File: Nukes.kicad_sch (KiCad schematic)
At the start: 25 parts, among them J12 Conn_01x05_Male, J6 Screw_Terminal_01x08, Q3 NCV8415STT1G, Q4 NCV8415STT1G, Q5 NCV8415STT1G, Q6 NCV8415STT1G, U4 LTV-247, U5 PCA9534RGVR, U6 PCA9685BS

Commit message: v2 time
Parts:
- C17: renamed from C7; footprint Capacitor_SMD:C_0603_1608Metric -> Capacitor_SMD:C_0402_1005Metric
- C18: renamed from C8; footprint Capacitor_SMD:C_0603_1608Metric -> Capacitor_SMD:C_0402_1005Metric
- C19: renamed from C9; footprint Capacitor_SMD:C_0603_1608Metric -> Capacitor_SMD:C_0402_1005Metric
- C20: renamed from C10; footprint Capacitor_SMD:C_0603_1608Metric -> Capacitor_SMD:C_0402_1005Metric
- D10: renamed from D8; footprint Diode_SMD:D_SOD-128 -> Package_TO_SOT_SMD:TO-277B
- D7: renamed from D16; footprint Diode_SMD:D_SOD-128 -> Package_TO_SOT_SMD:TO-277B
- D8: renamed from D10; footprint Diode_SMD:D_SOD-128 -> Package_TO_SOT_SMD:TO-277B
- D9: renamed from D15; footprint Diode_SMD:D_SOD-128 -> Package_TO_SOT_SMD:TO-277B
- renumbered J12 to J7, Q6 to Q2, Q4 to Q3, Q5 to Q4, Q3 to Q5, R34 to R17, R26 to R18, R36 to R19, R29 to R20, R33 to R21, R25 to R22, R27 to R23, R35 to R24, U4 to U3, U5 to U4, U6 to U5

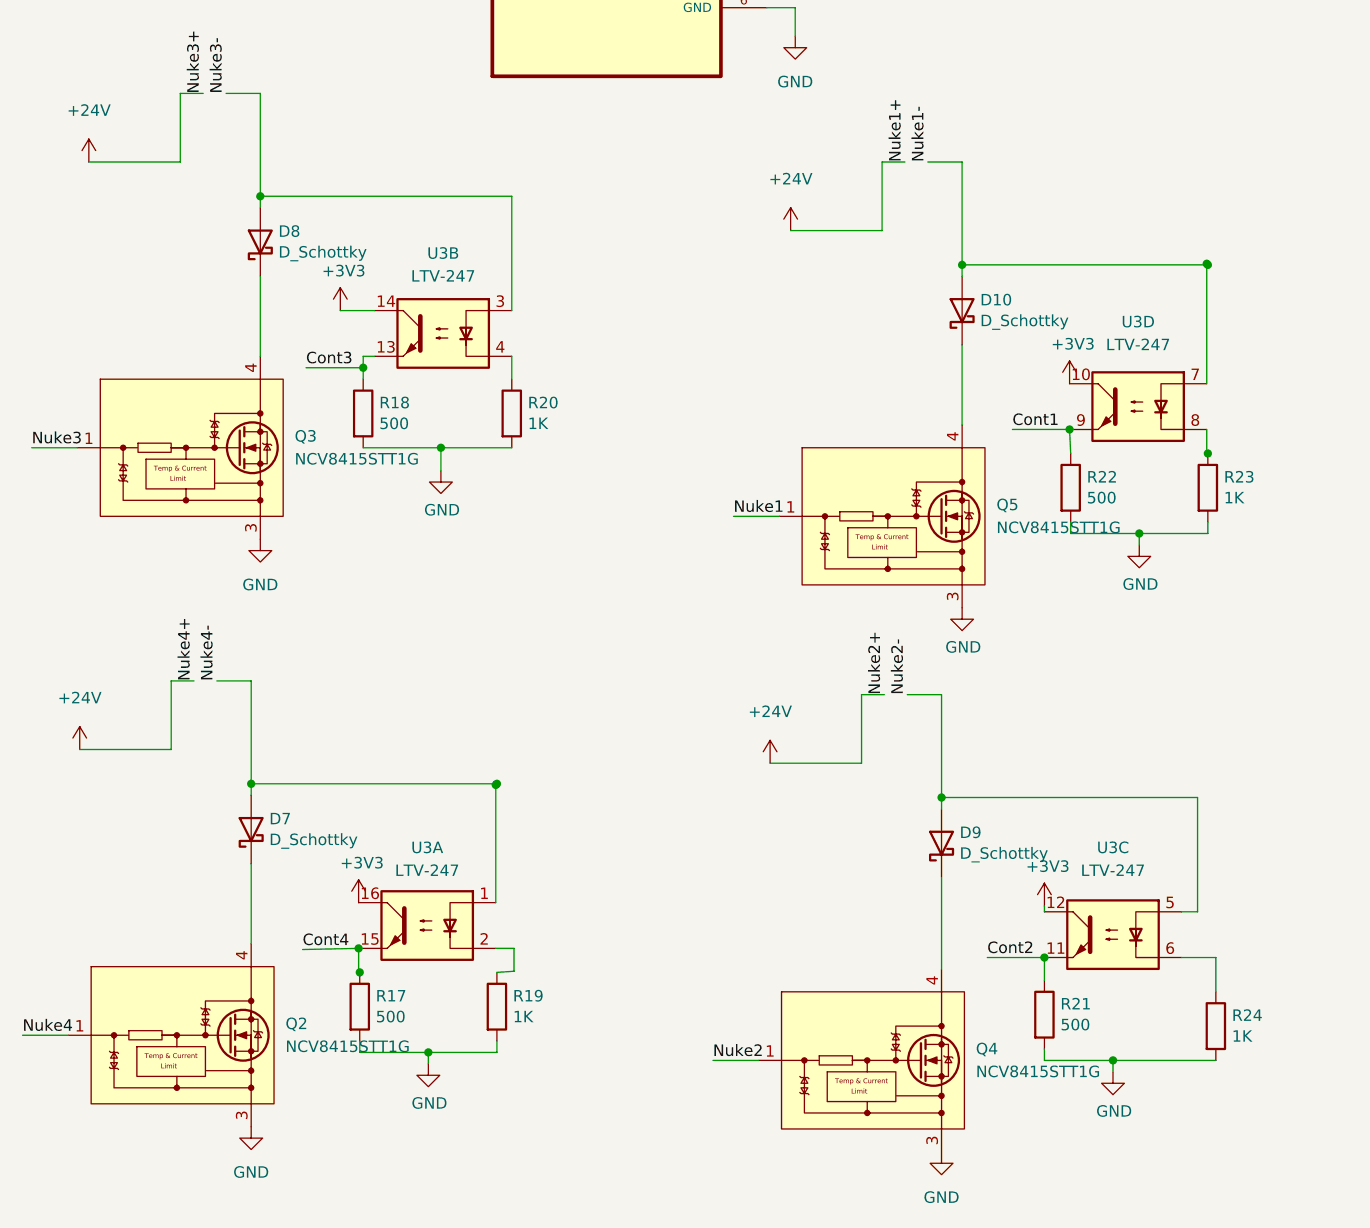
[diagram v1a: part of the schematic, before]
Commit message: Conitnued with v2, NB pinout of external sd card has changed!!! Chest needs to be updated before manufacturing!!!
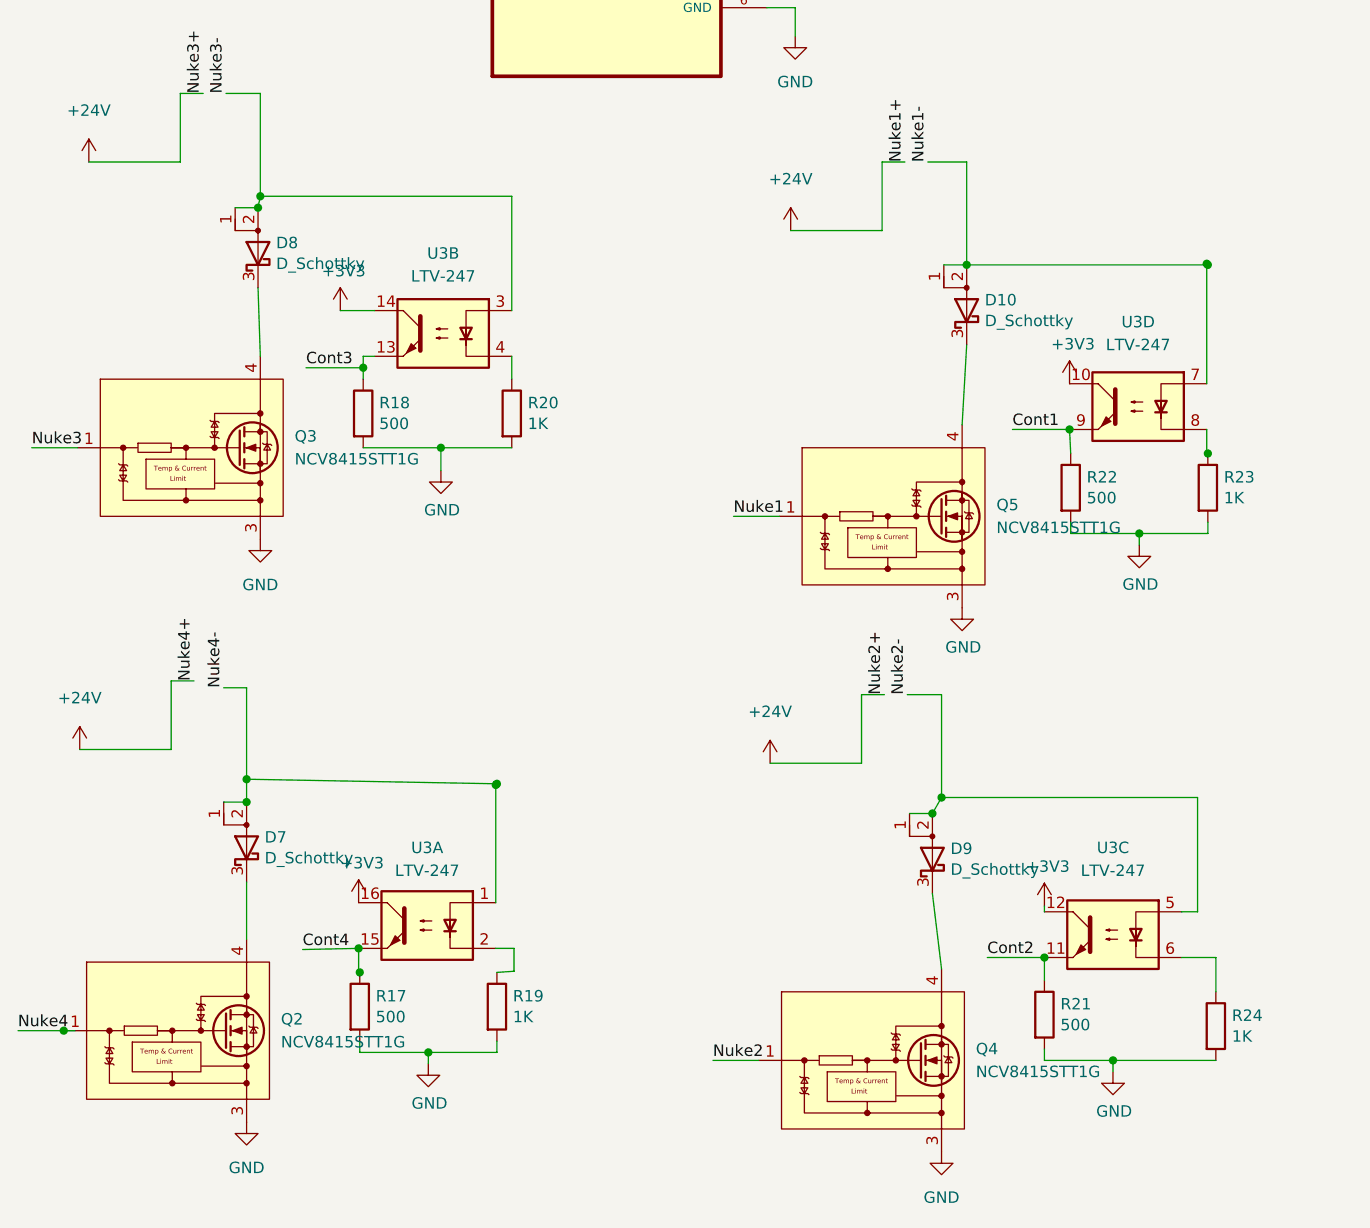
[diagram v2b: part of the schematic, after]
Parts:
- D10, D7, D8, D9: symbol Device:D_Schottky -> Device:D_Schottky_AAK
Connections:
- net Nuke1-: now also D10.1 (A)
- net Nuke2-: now also D9.1 (A)
- net Nuke3-: now also D8.1 (A)
- net Nuke4-: now also D7.1 (A)
- net at Q5.2 (D), Q5.4 (D): now also D10.3 (K); no longer D10.1 (K)
- net at Q2.2 (D), Q2.4 (D): now also D7.3 (K); no longer D7.1 (K)
- net at Q4.2 (D), Q4.4 (D): now also D9.3 (K); no longer D9.1 (K)
- net at Q3.2 (D), Q3.4 (D): now also D8.3 (K); no longer D8.1 (K)
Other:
- moved on the sheet: Q2

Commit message: made more progress
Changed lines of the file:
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@@
   (junction (at 60.96 113.03) (diameter 0) (color 0 0 0 0)
   )
+  (junction (at 119.253 92.71) (diameter 0) (color 0 0 0 0)
+  )
   (junction (at 67.056 150.495) (diameter 0) (color 0 0 0 0)
   )
   (junction (at 184.15 20.32) (diameter 0) (color 0 0 0 0)
   )
-  (junction (at 146.177 92.71) (diameter 0) (color 0 0 0 0)
-  )
   (junction (at 39.37 149.86) (diameter 0) (color 0 0 0 0)
   )
@@
   )
   (junction (at 166.37 64.77) (diameter 0) (color 0 0 0 0)
-  )
-  (junction (at 146.05 92.583) (diameter 0) (color 0 0 0 0)
   )
   (junction (at 146.177 113.665) (diameter 0) (color 0 0 0 0)
@@
     (stroke (width 0) (type default) (color 0 0 0 0))
   )
+  (wire (pts (xy 119.38 92.71) (xy 147.447 92.837))
+    (stroke (width 0) (type default) (color 0 0 0 0))
+  )
   (wire (pts (xy 39.37 161.29) (xy 39.37 167.64))
     (stroke (width 0) (type default) (color 0 0 0 0))
@@
     (stroke (width 0) (type default) (color 0 0 0 0))
   )
-  (wire (pts (xy 116.84 92.71) (xy 119.38 92.71))
+  (wire (pts (xy 116.84 92.71) (xy 119.253 92.71))
     (stroke (width 0) (type default) (color 0 0 0 0))
   )
@@
     (stroke (width 0) (type default) (color 0 0 0 0))
   )
+  (wire (pts (xy 119.253 92.71) (xy 119.38 92.71))
+    (stroke (width 0) (type default) (color 0 0 0 0))
+  )
   (wire (pts (xy 50.8 48.895) (xy 61.595 48.895))
     (stroke (width 0) (type default) (color 0 0 0 0))
@@
     (stroke (width 0) (type default) (color 0 0 0 0))
   )
+  (wire (pts (xy 148.59 106.045) (xy 146.05 105.918))
+    (stroke (width 0) (type default) (color 0 0 0 0))
+  )
   (wire (pts (xy 119.38 81.28) (xy 119.38 92.71))
     (stroke (width 0) (type default) (color 0 0 0 0))
@@
     (stroke (width 0) (type default) (color 0 0 0 0))
   )
-  (wire (pts (xy 146.05 92.583) (xy 146.177 92.71))
+  (wire (pts (xy 148.59 92.71) (xy 147.447 92.837))
     (stroke (width 0) (type default) (color 0 0 0 0))
   )
@@
     (stroke (width 0) (type default) (color 0 0 0 0))
   )
-  (wire (pts (xy 119.38 92.71) (xy 146.177 92.71))
-    (stroke (width 0) (type default) (color 0 0 0 0))
-  )
   (wire (pts (xy 98.552 120.65) (xy 93.472 120.65))
     (stroke (width 0) (type default) (color 0 0 0 0))
@@
     (stroke (width 0) (type default) (color 0 0 0 0))
   )
-  (wire (pts (xy 146.05 92.583) (xy 146.05 105.918))
-    (stroke (width 0) (type default) (color 0 0 0 0))
-  )
+  (wire (pts (xy 148.59 92.71) (xy 148.59 106.045))
+    (stroke (width 0) (type default) (color 0 0 0 0))
+  )

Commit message: all components basically routed and fitted onto pickle v2
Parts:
- R17, R18, R21, R22: footprint Resistor_SMD:R_0603_1608Metric -> Resistor_SMD:R_0402_1005Metric
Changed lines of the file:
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@@
       (effects (font (size 1.27 1.27)) (justify left))
     )
-    (property "Footprint" "Resistor_SMD:R_0603_1608Metric" (id 2) (at 129.159 117.475 90)
+    (property "Footprint" "Resistor_SMD:R_0402_1005Metric" (id 2) (at 129.159 117.475 90)
       (effects (font (size 1.27 1.27)) hide)
     )
@@
       (effects (font (size 1.27 1.27)) (justify left))
     )
-    (property "Footprint" "Resistor_SMD:R_0603_1608Metric" (id 2) (at 50.165 175.133 90)
+    (property "Footprint" "Resistor_SMD:R_0402_1005Metric" (id 2) (at 50.165 175.133 90)
       (effects (font (size 1.27 1.27)) hide)
     )
@@
       (effects (font (size 1.27 1.27)) (justify left))
     )
-    (property "Footprint" "Resistor_SMD:R_0603_1608Metric" (id 2) (at 126.238 176.022 90)
+    (property "Footprint" "Resistor_SMD:R_0402_1005Metric" (id 2) (at 126.238 176.022 90)
       (effects (font (size 1.27 1.27)) hide)
     )
@@
       (effects (font (size 1.27 1.27)) (justify left))
     )
-    (property "Footprint" "Resistor_SMD:R_0603_1608Metric" (id 2) (at 50.546 109.22 90)
-      (effects (font (size 1.27 1.27)) hide)
-    )
+    (property "Footprint" "Resistor_SMD:R_0402_1005Metric" (id 2) (at 50.546 109.22 90)
+      (effects (font (size 1.27 1.27)) hide)
+    )

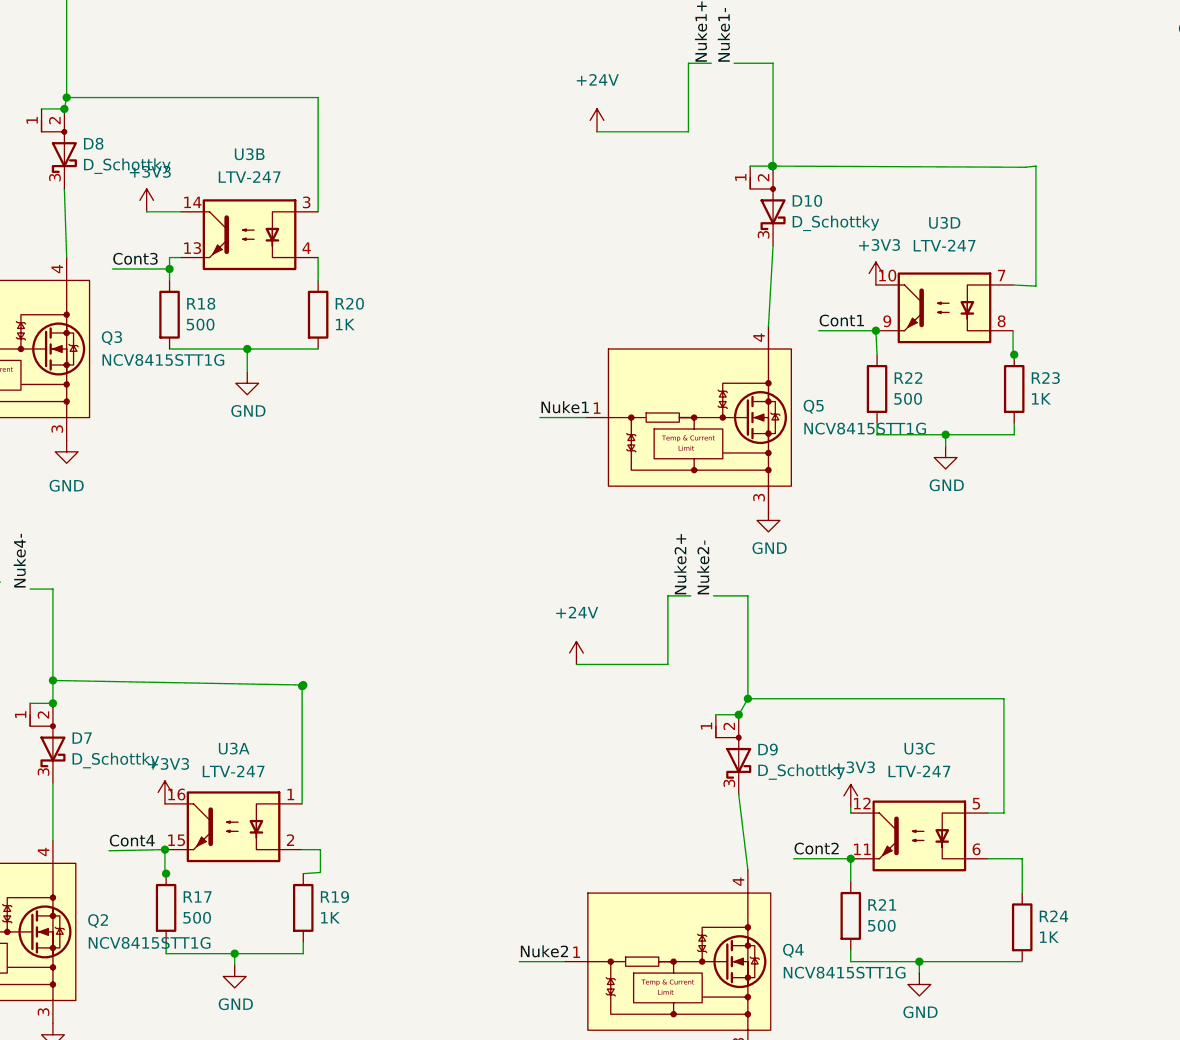
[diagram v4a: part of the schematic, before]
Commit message: changed bb and power side
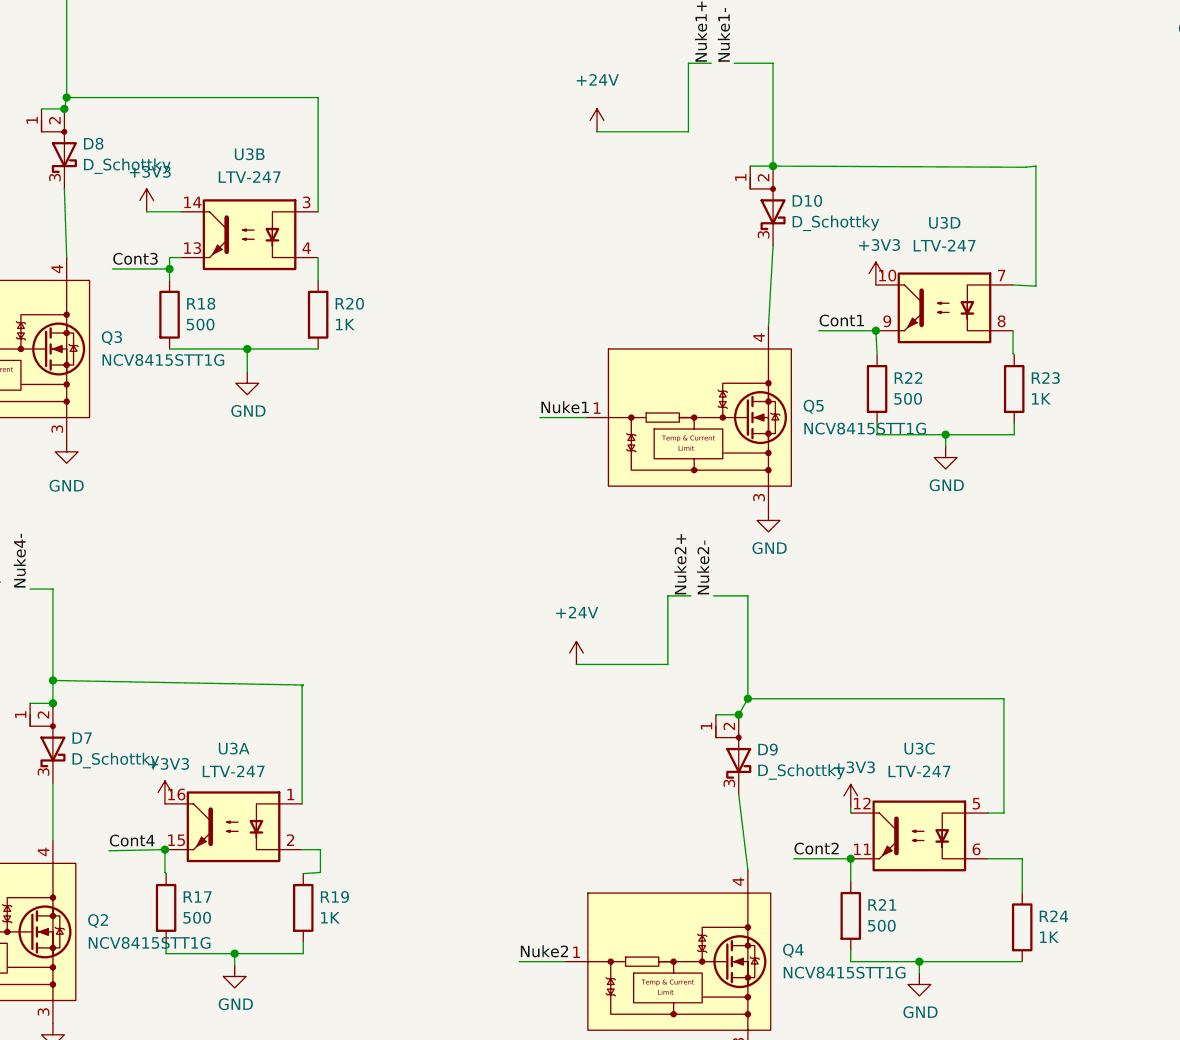
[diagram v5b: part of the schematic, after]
